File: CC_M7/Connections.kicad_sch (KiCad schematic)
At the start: 13 parts, among them J10 Conn_01x03_Pin, J11 USB_B_Micro, J12 Conn_01x05_Pin, J13 Conn_01x03_Pin, J14 Conn_01x04_Pin, J2 Conn_02x20_Odd_Even, J3 Conn_01x03_Pin, J4 Conn_01x03_Pin, J5 Conn_01x03_Pin, J6 Conn_01x03_Pin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

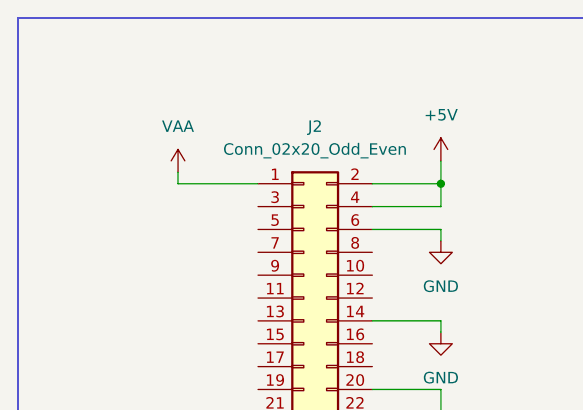
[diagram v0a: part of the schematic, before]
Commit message: label control
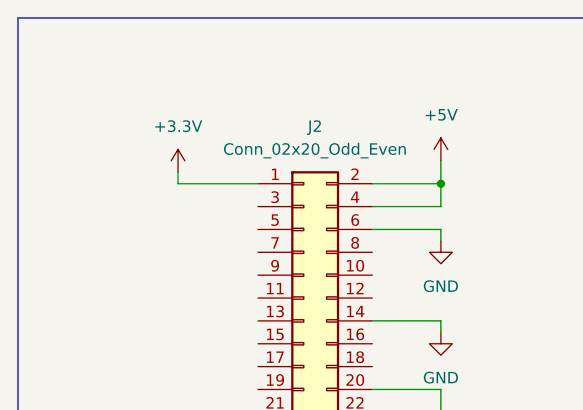
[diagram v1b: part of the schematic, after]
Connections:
- net VAA is gone; now on net +3.3V: J2.1 (Pin_1)
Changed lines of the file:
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@@
 		)
 	)
+	(global_label "SWDIO"
+		(shape input)
+		(at 52.07 68.58 0)
+		(fields_autoplaced yes)
+		(effects
+			(font
+				(size 1.27 1.27)
+			)
+			(justify left)
+		)
+		(property "Intersheetrefs" "${INTERSHEET_REFS}"
+			(at 60.9214 68.58 0)
+			(effects
+				(font
+					(size 1.27 1.27)
+				)
+				(justify left)
+				(hide yes)
+			)
+		)
+	)
 	(global_label "UART1_RX"
 		(shape input)
@@
 		)
 	)
-	(global_label "SWDIO"
-		(shape input)
-		(at 52.07 68.58 0)
-		(fields_autoplaced yes)
-		(effects
-			(font
-				(size 1.27 1.27)
-			)
-			(justify left)
-		)
-		(property "Intersheetrefs" "${INTERSHEET_REFS}"
-			(at 60.9214 68.58 0)
-			(effects
-				(font
-					(size 1.27 1.27)
-				)
-				(justify left)
-				(hide yes)
-			)
-		)
-	)
-	(global_label "SWCLK"
+	(global_label "UART1_TX"
 		(shape input)
-		(at 52.07 71.12 0)
+		(at 144.78 121.92 0)
 		(fields_autoplaced yes)
 		(effects
@@
 		)
 		(property "Intersheetrefs" "${INTERSHEET_REFS}"
-			(at 61.2842 71.12 0)
+			(at 156.7761 121.92 0)
 			(effects
 				(font
@@
 		)
 	)
-	(global_label "UART1_TX"
+	(global_label "Time_CH1"
 		(shape input)
-		(at 144.78 121.92 0)
+		(at 172.72 40.64 0)
 		(fields_autoplaced yes)
 		(effects
@@
 		)
 		(property "Intersheetrefs" "${INTERSHEET_REFS}"
-			(at 156.7761 121.92 0)
+			(at 184.8371 40.64 0)
 			(effects
 				(font
@@
 	(global_label "Time_CH1"
 		(shape input)
-		(at 172.72 40.64 0)
+		(at 132.08 19.05 0)
 		(fields_autoplaced yes)
 		(effects
@@
 		)
 		(property "Intersheetrefs" "${INTERSHEET_REFS}"
-			(at 184.8371 40.64 0)
+			(at 144.1971 19.05 0)
 			(effects
 				(font
@@
 		)
 	)
-	(global_label "Time_CH1"
+	(global_label "SWCLK"
 		(shape input)
-		(at 132.08 19.05 0)
+		(at 52.07 71.12 0)
 		(fields_autoplaced yes)
 		(effects
@@
 		)
 		(property "Intersheetrefs" "${INTERSHEET_REFS}"
-			(at 144.1971 19.05 0)
+			(at 61.2842 71.12 0)
 			(effects
 				(font
@@
 	)
 	(symbol
-		(lib_id "power:VAA")
-		(at 30.48 29.21 0)
-		(unit 1)
-		(exclude_from_sim no)
-		(in_bom yes)
-		(on_board yes)
-		(dnp no)
-		(fields_autoplaced yes)
-		(property "Reference" "#PWR041"
-			(at 30.48 33.02 0)
-			(effects
-				(font
-					(size 1.27 1.27)
-				)
-				(hide yes)
-			)
-		)
-		(property "Value" "VAA"
-			(at 30.48 24.13 0)
-			(effects
-				(font
-					(size 1.27 1.27)
-				)
-			)
-		)
-		(property "Footprint" ""
-			(at 30.48 29.21 0)
-			(effects
-				(font
-					(size 1.27 1.27)
-				)
-				(hide yes)
-			)
-		)
-		(property "Datasheet" ""
-			(at 30.48 29.21 0)
-			(effects
-				(font
-					(size 1.27 1.27)
-				)
-				(hide yes)
-			)
-		)
-		(property "Description" "Power symbol creates a global label with name \"VAA\""
-			(at 30.48 29.21 0)
-			(effects
-				(font
-					(size 1.27 1.27)
-				)
-				(hide yes)
-			)
-		)
-		(pin "1"
-		)
-		(instances
-			(project ""
-				(path "/20c3bbae-00c6-470e-8b69-dc0f665257a3/8b74e690-9be2-433b-8a0a-5eb3a275b61f"
-					(reference "#PWR041")
-					(unit 1)
-				)
-			)
-		)
-	)
-	(symbol
 		(lib_id "power:GND")
 		(at 64.77 67.31 0)
@@
 					(unit 1)
 				)
+			)
+		)
+	)
+	(symbol
+		(lib_id "power:+3.3V")
+		(at 30.48 29.21 0)
+		(unit 1)
+		(exclude_from_sim no)
+		(in_bom yes)
+		(on_board yes)
+		(dnp no)
+		(fields_autoplaced yes)
+		(property "Reference" "#PWR041"
+			(at 30.48 33.02 0)
+			(effects
+				(font
+					(size 1.27 1.27)
+				)
+				(hide yes)
+			)
+		)
+		(property "Value" "+3.3V"
+			(at 30.48 24.13 0)
+			(effects
+				(font
+					(size 1.27 1.27)
+				)
+			)
+		)
+		(property "Footprint" ""
+			(at 30.48 29.21 0)
+			(effects
+				(font
+					(size 1.27 1.27)
+				)
+				(hide yes)
+			)
+		)
+		(property "Datasheet" ""
+			(at 30.48 29.21 0)
+			(effects
+				(font
+					(size 1.27 1.27)
+				)
+				(hide yes)
+			)
+		)
+		(property "Description" "Power symbol creates a global label with name \"+3.3V\""
+			(at 30.48 29.21 0)
+			(effects
+				(font
+					(size 1.27 1.27)
+				)
+				(hide yes)
+			)
+		)
+		(pin "1"
+		)
+		(instances
+			(project ""
+				(path "/20c3bbae-00c6-470e-8b69-dc0f665257a3/8b74e690-9be2-433b-8a0a-5eb3a275b61f"
+					(reference "#PWR041")
+					(unit 1)
+				)

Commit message: Connectors updated
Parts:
- removed J10, J13, J9: Conn_01x03_Pin, symbol Connector:Conn_01x03_Pin
- removed J14: Conn_01x04_Pin, symbol Connector:Conn_01x04_Pin
- added J16: Conn_01x06_Pin, symbol Connector:Conn_01x06_Pin
- added J17: Conn_01x04_Pin, symbol Connector:Conn_01x04_Pin
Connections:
- net +5V: now also J16.1 (Pin_1), J17.1 (Pin_1)
- net GND: now also J8.3 (Pin_3), J16.6 (Pin_6), J17.4 (Pin_4)
- removed net Time_CH1: J3.1 (Pin_1), J4.1 (Pin_1), J5.1 (Pin_1), J6.1 (Pin_1), J7.1 (Pin_1), J8.1 (Pin_1)
- net USB_D+ renamed USB_DP
- net USB_D- renamed USB_DM
- new net ADC1_VS: J17.2 (Pin_2)
- new net ADC2_AS: J17.3 (Pin_3)
- new net TIM3_CH1: J6.1 (Pin_1)
- new net TIM3_CH2: J5.1 (Pin_1)
- new net TIM3_CH3: J4.1 (Pin_1)
- new net TIM3_CH4: J3.1 (Pin_1)
- new net TIM4_CH3: J8.1 (Pin_1)
- new net TIM4_CH4: J7.1 (Pin_1)
- new net TRX1_CTS: J16.4 (Pin_4)
- new net TRX1_RTS: J16.5 (Pin_5)
- new net UART3_RX: J16.3 (Pin_3)
- new net UART3_TX: J16.2 (Pin_2)
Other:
- note added: "POWER CONN"
- note added: "PWM PINS"
- note added: "TRX CONN"
- note added: "YENIAY"
- note removed: "CAN CONN"
- note removed: "PPM CONN"
- note removed: "PWN PINS"
- company: YENİAY -> (none)
- moved on the sheet: J11, J12

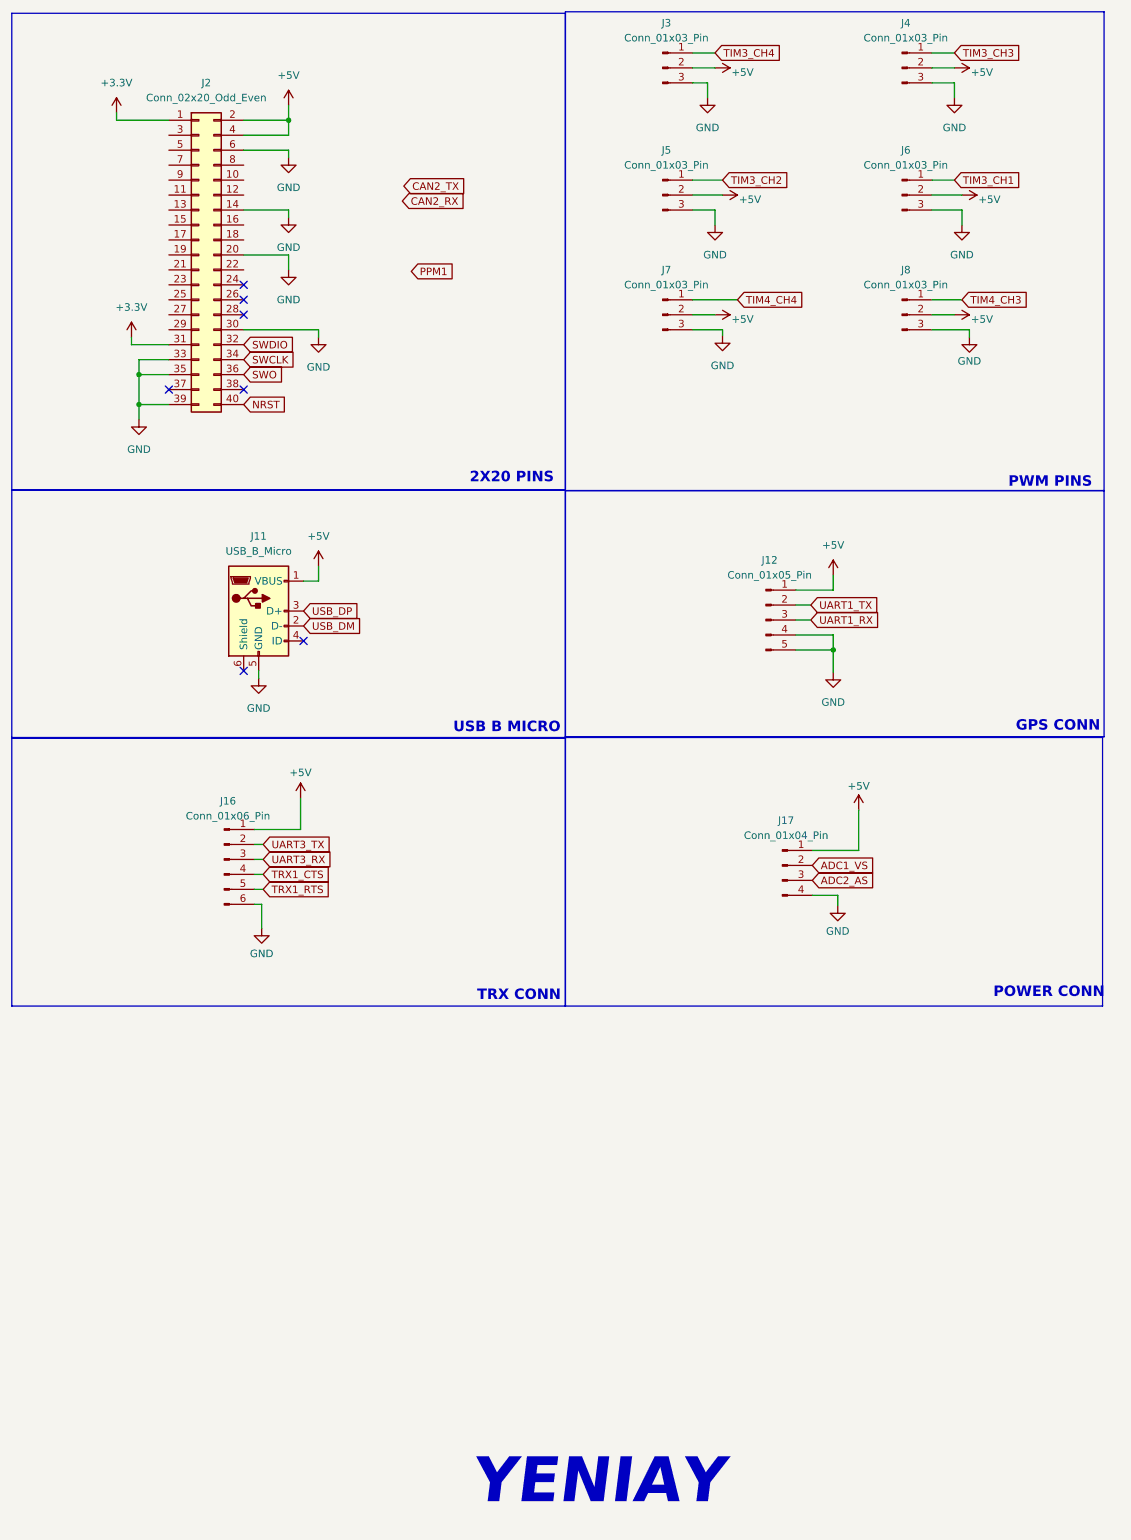
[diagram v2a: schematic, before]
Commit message: NRF pins updated
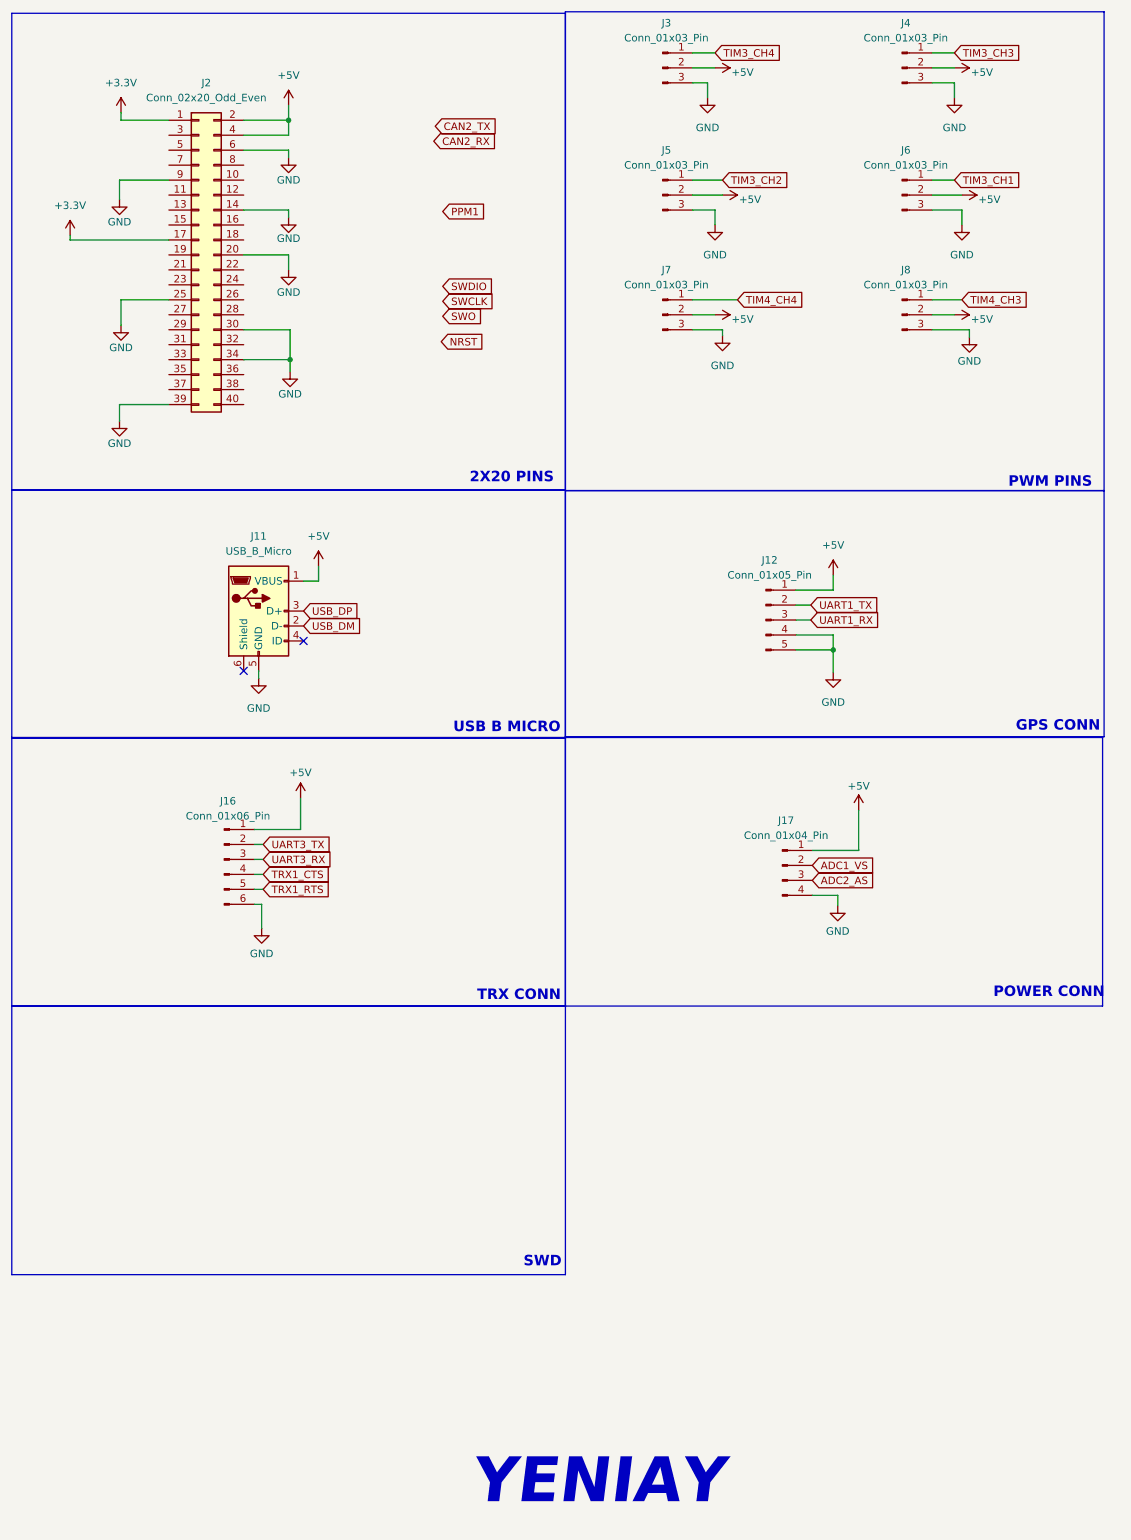
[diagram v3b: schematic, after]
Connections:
- net +3.3V: now also J2.17 (Pin_17); no longer J2.31 (Pin_31)
- net GND: now also J2.25 (Pin_25), J2.34 (Pin_34), J2.9 (Pin_9); no longer J2.33 (Pin_33), J2.35 (Pin_35)
- net NRST: no longer J2.40 (Pin_40)
- net SWCLK: no longer J2.34 (Pin_34)
- net SWDIO: no longer J2.32 (Pin_32)
- net SWO: no longer J2.36 (Pin_36)
- no-connect marks 7 -> 2
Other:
- note added: "SWD"

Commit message: final schematic 6 warning
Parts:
- J2: value Conn_02x20_Odd_Even -> ~
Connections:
- net CAN2_RX: now also J2.13 (Pin_13)
- net CAN2_TX: now also J2.15 (Pin_15)
- net UART2_TX: now reaches J2.10 (Pin_10)
- net PA1: now reaches J2.11 (Pin_11)
- net PA0: now reaches J2.12 (Pin_12)
- net UART4_RX: now reaches J2.16 (Pin_16)
- net UART4_TX: now reaches J2.18 (Pin_18)
- net SPI1_MOSI: now reaches J2.19 (Pin_19)
- net SPI1_MISO: now reaches J2.21 (Pin_21)
- net PC15: now reaches J2.22 (Pin_22)
- net SPI1_SCK: now reaches J2.23 (Pin_23)
- net PC14: now reaches J2.24 (Pin_24)
- net PC13: now reaches J2.26 (Pin_26)
- net PE6: now reaches J2.29 (Pin_29)
- net I2C2_SDA: now reaches J2.3 (Pin_3)
- net PE5: now reaches J2.31 (Pin_31)
- net J2_32: now reaches J2.32 (Pin_32)
- net PE4: now reaches J2.33 (Pin_33)
- net PE3: now reaches J2.35 (Pin_35)
- net J2_36: now reaches J2.36 (Pin_36)
- net PE2: now reaches J2.37 (Pin_37)
- net J2_38: now reaches J2.38 (Pin_38)
- net J2_40: now reaches J2.40 (Pin_40)
- net I2C2_SCL: now reaches J2.5 (Pin_5)
- net PA4: now reaches J2.7 (Pin_7)
- net UART2_RX: now reaches J2.8 (Pin_8)
- no-connect marks 2 -> 4
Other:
- moved on the sheet: J11, J16, J17
